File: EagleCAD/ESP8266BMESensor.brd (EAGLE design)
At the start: 55 x 30 mm, 21 parts, among them J1 AMP FCI 10103594-0001LF

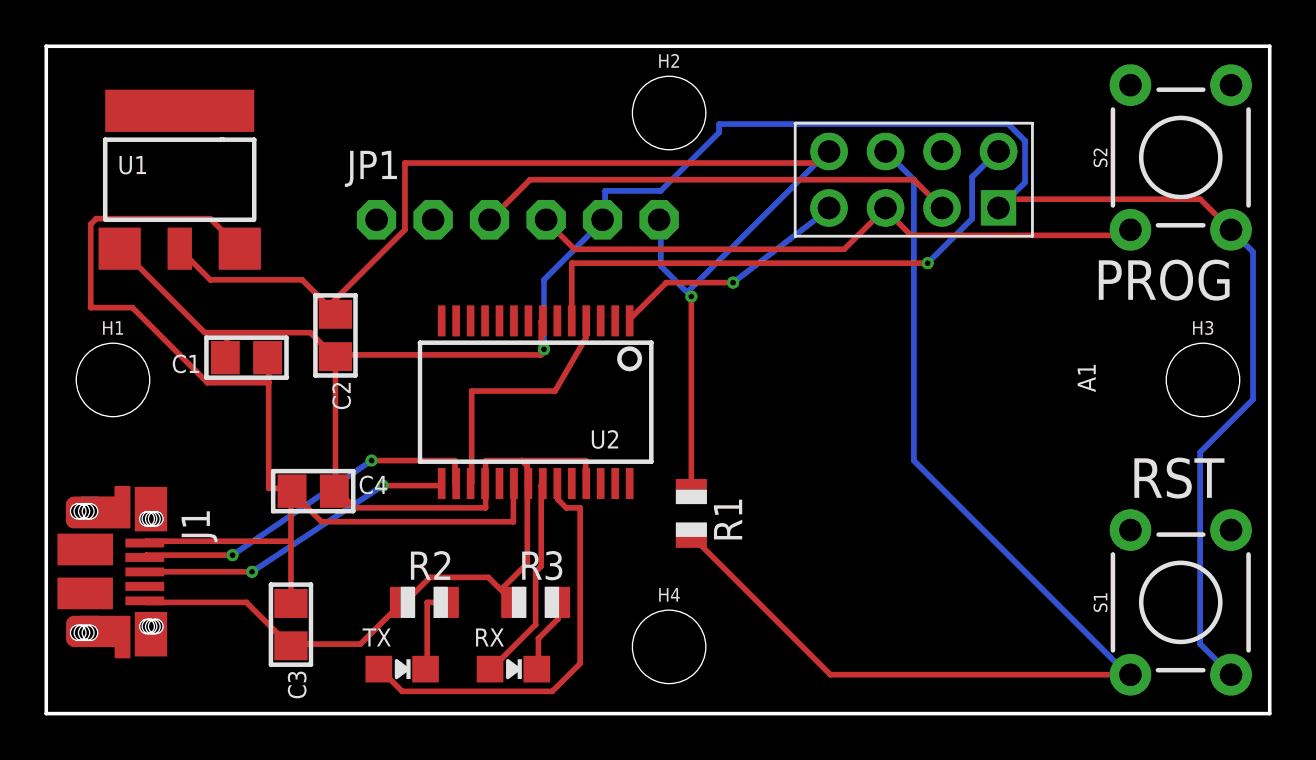
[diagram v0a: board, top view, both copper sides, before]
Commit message: updating PCB and adding USB to UART IC
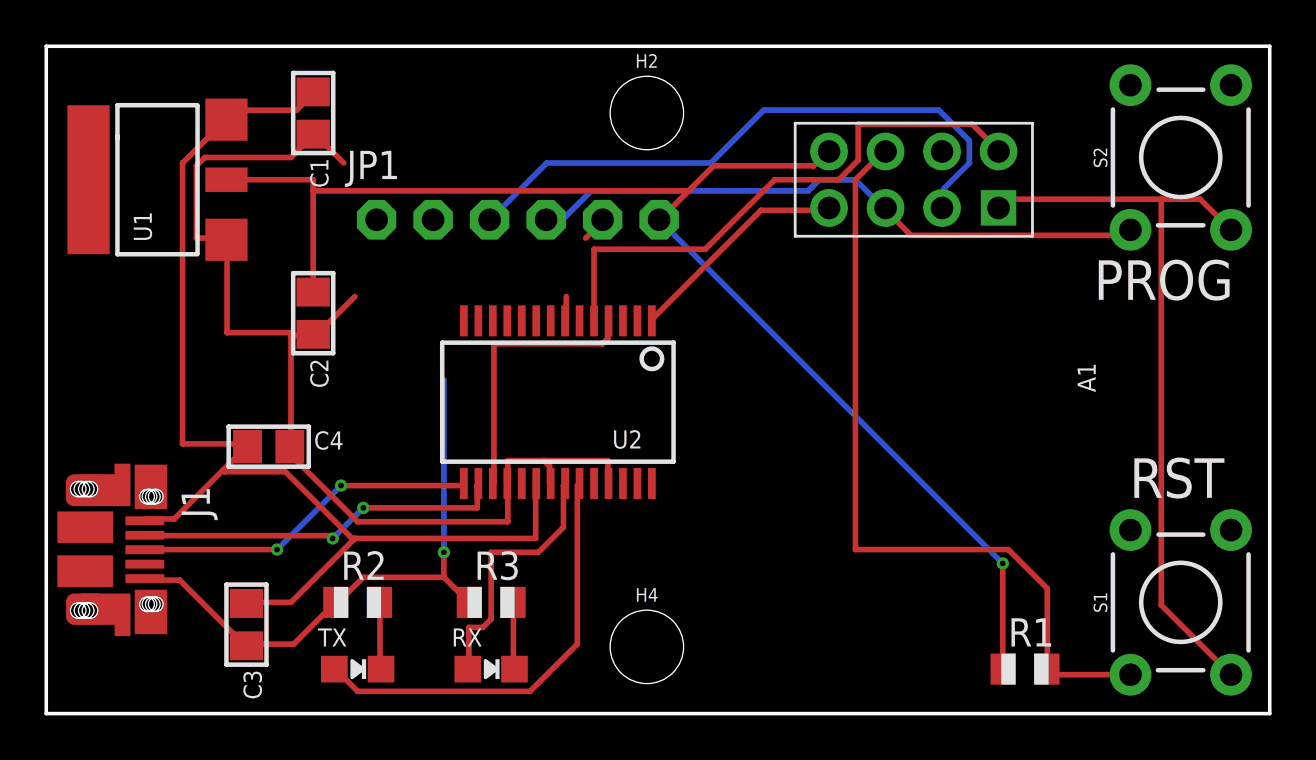
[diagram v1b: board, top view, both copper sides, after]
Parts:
- removed H1, H3: STAND-OFF, SparkFun-Hardware:STAND-OFF
- moved R1 16.6 mm to (44.0, 2.00), turned to 0 degrees
- moved C1 11.4 mm to (12.0, 27.0), turned to 270 degrees
- moved R2 3.00 mm to (14.0, 5.00)
- moved C4 2.83 mm to (10.0, 12.0)
- moved C3 2.00 mm to (9.00, 4.00)
- moved R3 2.00 mm to (20.0, 5.00)
- moved TX 2.00 mm to (14.0, 2.00)
- moved C2 1.41 mm to (12.0, 18.0)
- moved H2 1.00 mm to (27.0, 27.0)
- moved H4 1.00 mm to (27.0, 3.00)
- moved J1 1.00 mm to (3.10, 7.40)
- moved RX 1.00 mm to (20.0, 2.00)
- moved U1 1.00 mm to (5.00, 24.0), turned to 90 degrees
- moved U2 1.00 mm to (23.0, 14.0)
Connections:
- net N$4 renamed VCCIO
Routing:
- net GND: track 136.8 -> 111.8 mm
- net RST: track 50.5 -> 35.3 mm
- net SCL: track 21.6 -> 27.7 mm
- net 3.3V: track 57.8 -> 61.3 mm
- net RXLED: track 9.35 -> 11.8 mm
- net +5V: track 51.6 -> 52.8 mm
- net USB+: track 14.6 -> 15.6 mm
- net N$2: track 3.95 -> 3.05 mm
- net VCCIO: track 11.5 -> 12.3 mm
- net RX: track 10.9 -> 10.1 mm, vias 1 -> 0
- net TXLED: track 18.9 -> 19.5 mm
- net TX: track 25.0 -> 25.2 mm, vias 1 -> 0

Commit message: fixinng SDA/SCL pins and setting MQTT update to 5 mins
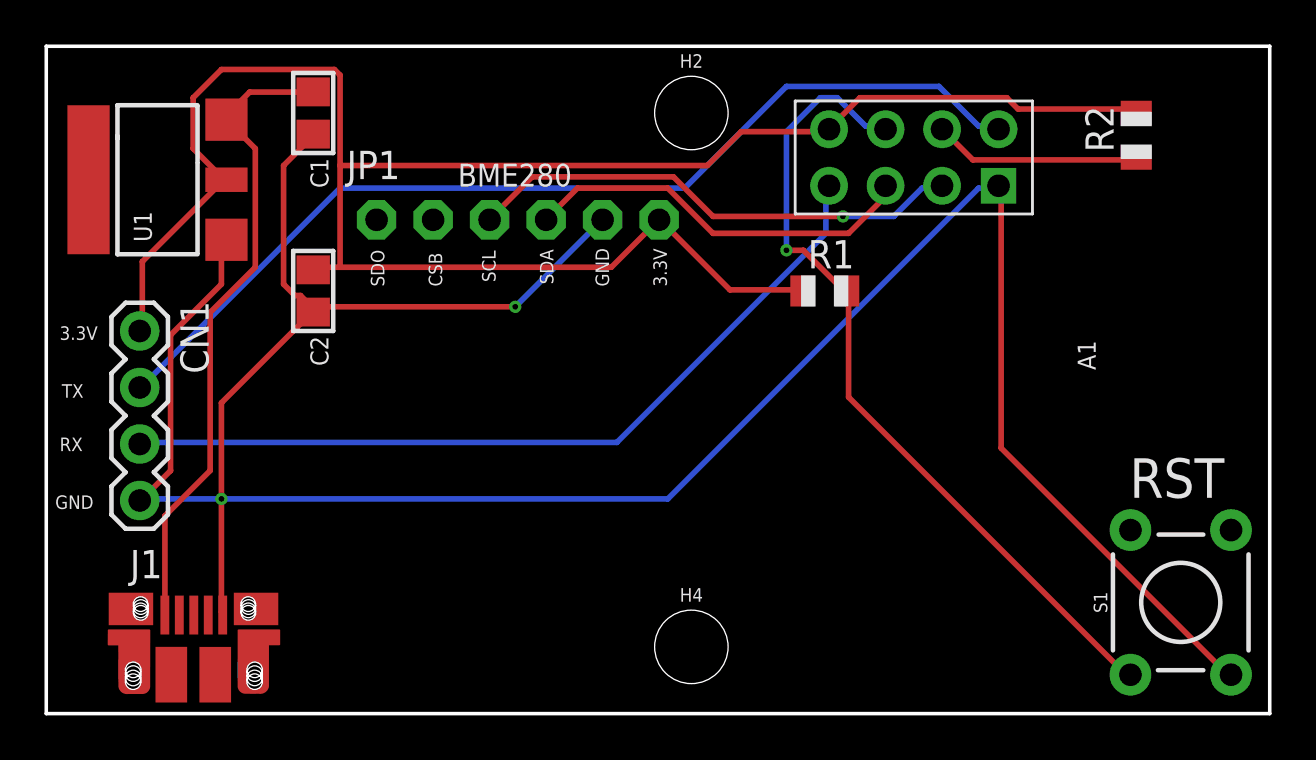
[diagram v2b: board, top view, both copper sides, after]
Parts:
- removed C3: 0.1uF, microbuilder:0805
- removed C4: 10uF, microbuilder:0805
- removed R3: 330, adafruit:R0805
- removed RX, TX: (no value), microbuilder:CHIPLED_0805_NOOUTLINE
- removed S2: MOMENTARY-SWITCH-SPST-PTH-6.0MM, SparkFun-Switches:TACTILE_SWITCH_PTH_6.0MM
- removed U2: (no value), microbuilder:SSOP28DB
- added CN1: 1X4-BIG, adafruit:1X04-BIG
- R2: value 330 -> (none)
- moved R2 40.8 mm to (49.0, 26.0), turned to 90 degrees
- moved R1 19.2 mm to (35.0, 19.0)
- moved J1 5.54 mm to (6.60, 3.10), turned to 0 degrees
- moved H2 2.00 mm to (29.0, 27.0)
- moved H4 2.00 mm to (29.0, 3.00)
- moved A1 1.00 mm to (39.0, 25.0)
- moved C2 1.00 mm to (12.0, 19.0)
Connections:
- removed net N$2: R2.2, TX.C
- removed net N$3: R3.2, RX.C
- removed net RXLED: RX.A, U2.22
- removed net TXLED: TX.A, U2.23
- removed net USB+: J1.D+, U2.15
- removed net USB-: J1.D-, U2.16
- removed net VCCIO: U2.17, U2.4
- net +5V: no longer C3.1, C4.1, U2.20
- net 3.3V: now also CN1.1, R2.2
- net EN/CHPD: now also R2.1
- net GND: now also CN1.4; no longer C3.2, C4.2, R2.1, R3.1, S2.3, U2.18, U2.21, U2.25, U2.7
- net RX: now also CN1.3; no longer U2.1
- net SDA: no longer S2.1
- net TX: now also CN1.2; no longer U2.5
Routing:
- net 3.3V: track 61.3 -> 90.2 mm, vias 1 -> 0
- net RX: track 10.1 -> 37.0 mm
- net +5V: track 52.8 -> 29.0 mm
- net TX: track 25.2 -> 45.0 mm
- net TXLED: track 19.5 -> 0.00 mm
- net USB-: track 16.7 -> 0.00 mm, vias 2 -> 0
- net USB+: track 15.6 -> 0.00 mm, vias 2 -> 0
- net VCCIO: track 12.3 -> 0.00 mm
- net RXLED: track 11.8 -> 0.00 mm
- net GND: track 111.8 -> 123.5 mm, vias 1 -> 2
- net SDA: track 28.2 -> 17.9 mm
- net EN/CHPD: track 0.00 -> 9.32 mm
- net SCL: track 27.7 -> 22.4 mm, vias 0 -> 1
- net N$3: track 3.05 -> 0.00 mm
- net N$2: track 3.05 -> 0.00 mm
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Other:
- board text added: "3.3V"
- board text added: "BME280"
- board text added: "CSB"
- board text added: "GND"
- board text added: "RX"
- board text added: "SCL"
- board text added: "SDA"
- board text added: "SDO"
- board text added: "TX"
- board text added: "v1.5"
- board text removed: "PROG"
- board text removed: "v1.2"
